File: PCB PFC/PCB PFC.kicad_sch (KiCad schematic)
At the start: 48 parts, among them J4 External_Power, J5 JUMPER_BAT54S, SW2 SW_Push, U1 INA122, U3 TL082, U4 TL084, U5 TL082, U8 ESP32-C3_SUPERMINI_TH

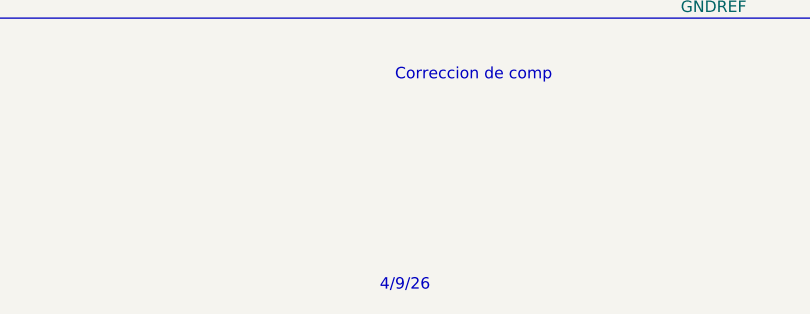
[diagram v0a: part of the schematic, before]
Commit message: v1.8.0: calibracion medida, trazabilidad de la escala y crudo de A0
Los ohms de esta version no son comparables con los de la 1.7.0: la escala
pasa de constantes de diseño a constantes medidas en banco. Conversion para
reportes viejos: Z_nueva = 0,3454*Z_vieja - 0,3718 (absolutos) y solo el
factor para diferencias.

El firmware reporta su K_CAL en el STATUS y la app etiqueta cada sesion con
la calibracion que realmente la midio. El PDF ahora dice con que se midio.
Se guarda la continua cruda de A0.

Ver Programacion_UI_Micro/UI_REACT/RELEASE_v1.8.0.md
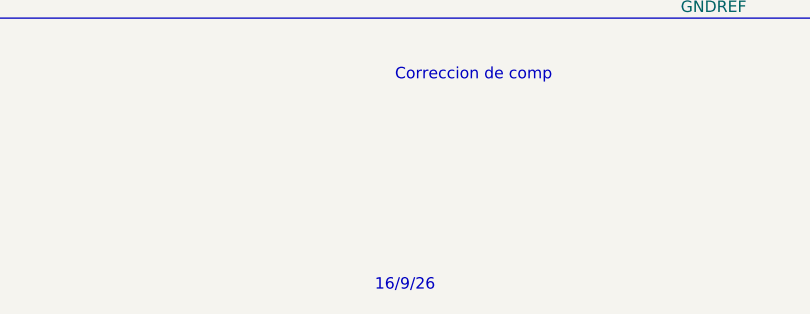
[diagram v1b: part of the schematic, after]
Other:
- note added: "16/9/26"
- note removed: "4/9/26"
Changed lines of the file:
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@@
 		)
 	)
-	(text "4/9/26"
+	(text "16/9/26"
 		(exclude_from_sim no)
 		(at 217.17 193.548 0)
